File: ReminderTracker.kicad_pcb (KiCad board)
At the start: 2 copper layers, 92 x 150 mm, 24 parts, among them J1 External RTC, SW1 SW_Push, SW2 SW_Push, SW3 SW_Push, SW4 SW_Push, SW5 SW_Push, SW6 SW_Push, U1 XIAO-ESP32-C3-DIP

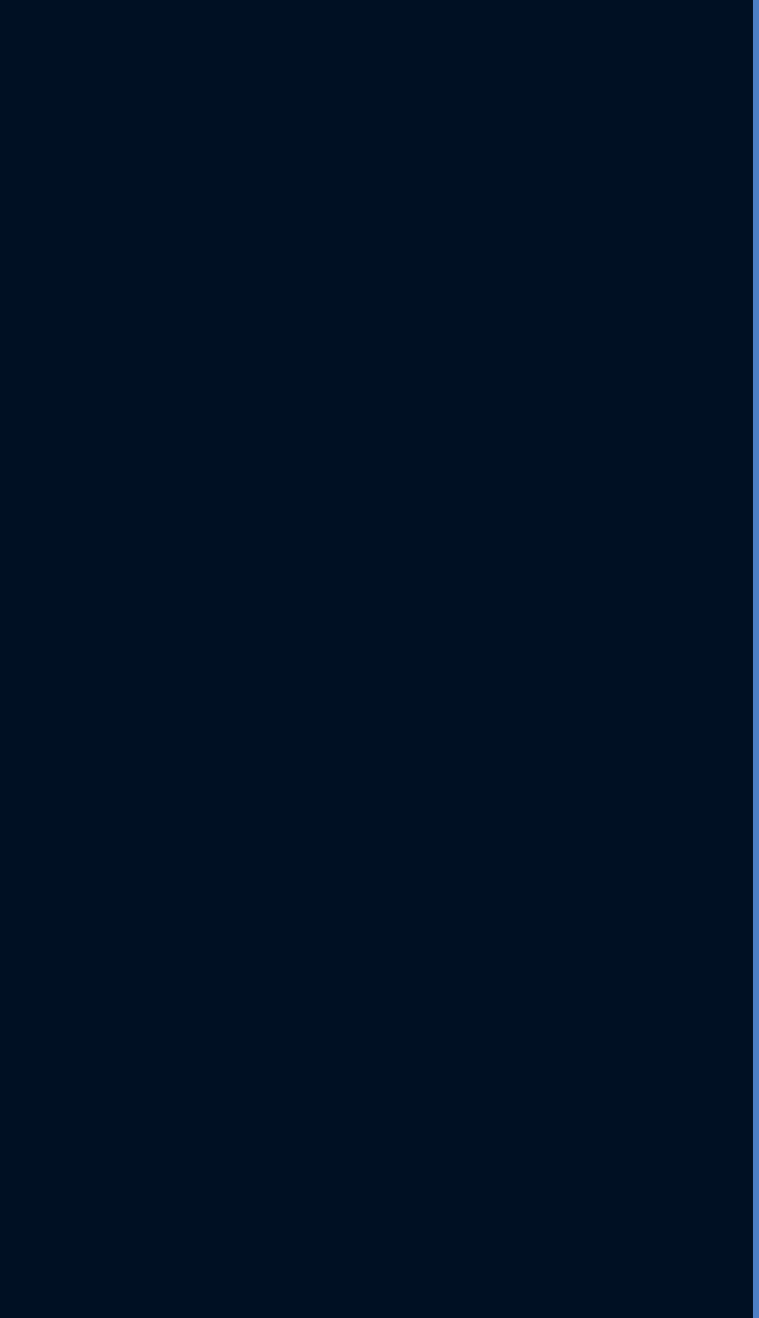
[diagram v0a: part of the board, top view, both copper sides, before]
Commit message: antenna cutout
Add antenna cutout and silkscreen
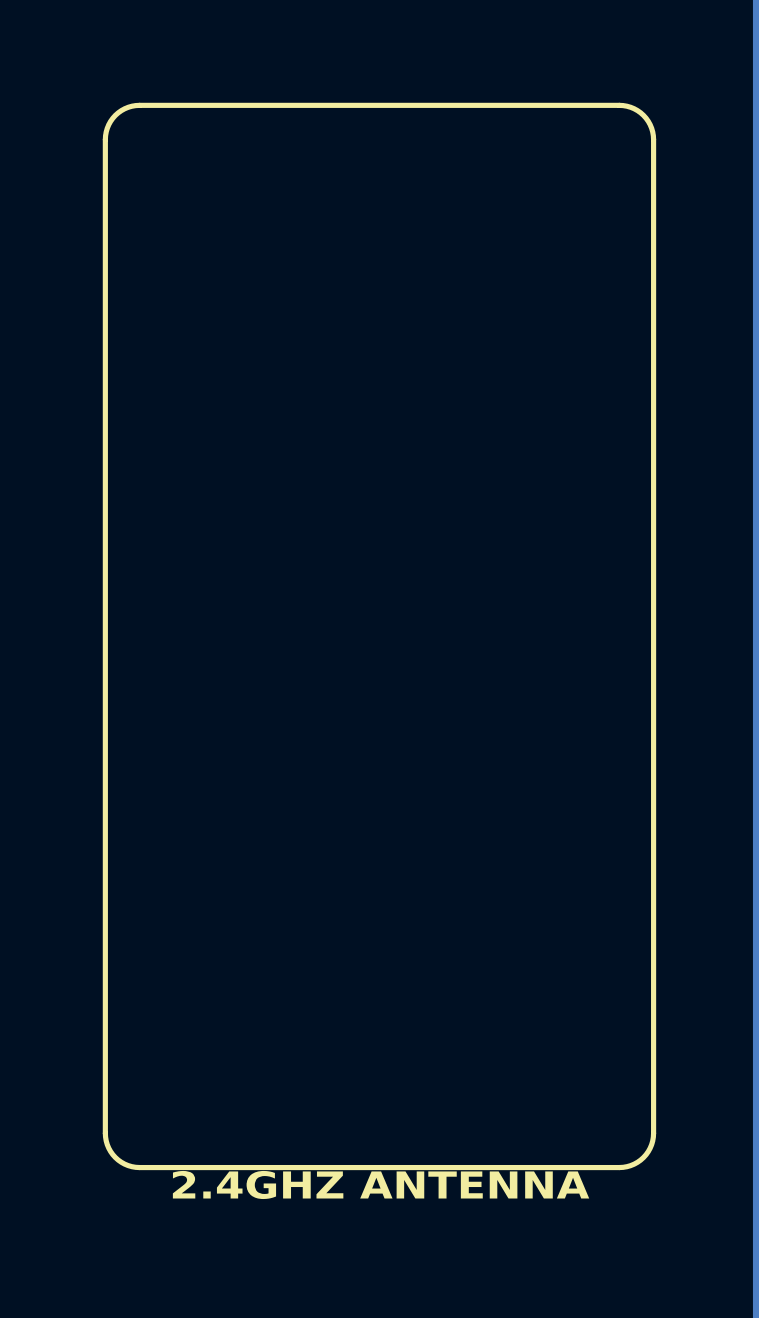
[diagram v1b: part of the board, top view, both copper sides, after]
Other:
- board text added: "2.4GHZ ANTENNA"
